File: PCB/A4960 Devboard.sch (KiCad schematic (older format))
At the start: 56 parts, among them IC1 ATMEGA8-AI, P1 CONN_02X03, P2 CONN_01X02, P3 CONN_01X03, P4 CONN_01X03, Q1 Q_NMOS_GDS_old, Q2 Q_NMOS_GDS_old, Q3 Q_NMOS_GDS_old, Q4 Q_NMOS_GDS_old, Q5 Q_NMOS_GDS_old, Q6 Q_NMOS_GDS_old, U1 LM2931AZ-5.0, U2 A4960, Y1 16MHz

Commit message: PCB weiter gemcht & neuer Spannungswandler auf 5V
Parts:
- removed U1: LM2931AZ-5.0, toni:SOT223_GND_VO_VI, symbol LM2931AZ-5.0
- added U1: LD1117S50TR, TO_SOT_Packages_SMD:SOT-223, symbol LD1117S50TR
- R13: footprint Resistors_SMD:R_0603 -> Resistors_SMD:R_2512
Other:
- moved on the sheet: R20
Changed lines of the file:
@@
 F 0 "R13" V 7380 4600 50  0000 C CNN
 F 1 "R" V 7300 4600 50  0000 C CNN
-F 2 "Resistors_SMD:R_0603" V 7230 4600 30  0001 C CNN
+F 2 "Resistors_SMD:R_2512" V 7230 4600 30  0001 C CNN
 F 3 "" H 7300 4600 30  0000 C CNN
 	1    7300 4600
@@
 $EndComp
 $Comp
-L LM2931AZ-5.0 U1
-U 1 1 5653AFAA
-P 2400 6725
-F 0 "U1" H 2400 6975 40  0000 C CNN
-F 1 "LM2931AZ-5.0" H 2400 6925 40  0000 C CNN
-F 2 "toni:SOT223_GND_VO_VI" H 2400 6825 35  0001 C CIN
-F 3 "" H 2400 6725 60  0000 C CNN
-	1    2400 6725
-	1    0    0    -1
-$EndComp
-$Comp
 L +3.3V #PWR050
 U 1 1 5653B466
-P 2800 6675
-F 0 "#PWR050" H 2800 6525 50  0001 C CNN
-F 1 "+3.3V" H 2800 6815 50  0000 C CNN
-F 2 "" H 2800 6675 60  0000 C CNN
-F 3 "" H 2800 6675 60  0000 C CNN
-	1    2800 6675
+P 2675 6125
+F 0 "#PWR050" H 2675 5975 50  0001 C CNN
+F 1 "+3.3V" H 2675 6265 50  0000 C CNN
+F 2 "" H 2675 6125 60  0000 C CNN
+F 3 "" H 2675 6125 60  0000 C CNN
+	1    2675 6125
 	1    0    0    -1
 $EndComp
@@
 L GND #PWR051
 U 1 1 5653BE8A
-P 2400 6975
-F 0 "#PWR051" H 2400 6725 50  0001 C CNN
-F 1 "GND" H 2400 6825 50  0000 C CNN
-F 2 "" H 2400 6975 60  0000 C CNN
-F 3 "" H 2400 6975 60  0000 C CNN
-	1    2400 6975
+P 2275 6425
+F 0 "#PWR051" H 2275 6175 50  0001 C CNN
+F 1 "GND" H 2275 6275 50  0000 C CNN
+F 2 "" H 2275 6425 60  0000 C CNN
+F 3 "" H 2275 6425 60  0000 C CNN
+	1    2275 6425
 	1    0    0    -1
 $EndComp
@@
 L VPP #PWR052
 U 1 1 5653BF3A
-P 1700 6675
-F 0 "#PWR052" H 1700 6525 50  0001 C CNN
-F 1 "VPP" H 1700 6825 50  0000 C CNN
-F 2 "" H 1700 6675 60  0000 C CNN
-F 3 "" H 1700 6675 60  0000 C CNN
-	1    1700 6675
+P 1575 6125
+F 0 "#PWR052" H 1575 5975 50  0001 C CNN
+F 1 "VPP" H 1575 6275 50  0000 C CNN
+F 2 "" H 1575 6125 60  0000 C CNN
+F 3 "" H 1575 6125 60  0000 C CNN
+	1    1575 6125
 	0    -1   -1   0
 $EndComp
@@
 L R R20
 U 1 1 5653BFEC
-P 1850 6675
-F 0 "R20" V 1930 6675 50  0000 C CNN
-F 1 "1" V 1850 6675 50  0000 C CNN
-F 2 "Resistors_SMD:R_0805" V 1780 6675 30  0001 C CNN
-F 3 "" H 1850 6675 30  0000 C CNN
-	1    1850 6675
+P 1725 6125
+F 0 "R20" V 1805 6125 50  0000 C CNN
+F 1 "1" V 1725 6125 50  0000 C CNN
+F 2 "Resistors_SMD:R_0805" V 1655 6125 30  0001 C CNN
+F 3 "" H 1725 6125 30  0000 C CNN
+	1    1725 6125
 	0    1    1    0
 $EndComp
@@
 $EndComp
 $Comp
-L +3.3V #PWR?
+L +3.3V #PWR054
 U 1 1 56577063
 P 4550 2950
-F 0 "#PWR?" H 4550 2800 50  0001 C CNN
+F 0 "#PWR054" H 4550 2800 50  0001 C CNN
 F 1 "+3.3V" H 4550 3090 50  0000 C CNN
 F 2 "" H 4550 2950 60  0000 C CNN
@@
 $EndComp
 Connection ~ 4600 2950
+$Comp
+L LD1117S50TR U1
+U 1 1 565871BF
+P 2275 6175
+F 0 "U1" H 2275 6425 40  0000 C CNN
+F 1 "LD1117S50TR" H 2275 6375 40  0000 C CNN
+F 2 "TO_SOT_Packages_SMD:SOT-223" H 2275 6275 40  0000 C CNN
+F 3 "" H 2275 6175 60  0000 C CNN
+	1    2275 6175
+	1    0    0    -1
+$EndComp
 $EndSCHEMATC

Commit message: PCB fertig!
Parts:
- Q1, Q2, Q3, Q4, Q5, Q6: footprint sven:SO8_WITH_Heatpipes -> Sven:SO8_WITH_Heatpipes_New
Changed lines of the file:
@@
 F 0 "Q1" H 9350 2750 50  0000 R CNN
 F 1 "Q_NMOS_GDS_old" H 9700 2650 50  0000 R CNN
-F 2 "sven:SO8_WITH_Heatpipes" H 9250 2800 29  0001 C CNN
+F 2 "Sven:SO8_WITH_Heatpipes_New" H 9250 2800 29  0001 C CNN
 F 3 "" H 9050 2700 60  0000 C CNN
 	1    9050 2700
@@
 F 0 "Q2" H 9350 3150 50  0000 R CNN
 F 1 "Q_NMOS_GDS_old" H 9700 3050 50  0000 R CNN
-F 2 "sven:SO8_WITH_Heatpipes" H 9250 3200 29  0001 C CNN
+F 2 "Sven:SO8_WITH_Heatpipes_New" H 9250 3200 29  0001 C CNN
 F 3 "" H 9050 3100 60  0000 C CNN
 	1    9050 3100
@@
 F 0 "Q3" H 9350 3850 50  0000 R CNN
 F 1 "Q_NMOS_GDS_old" H 9700 3750 50  0000 R CNN
-F 2 "sven:SO8_WITH_Heatpipes" H 9250 3900 29  0001 C CNN
+F 2 "Sven:SO8_WITH_Heatpipes_New" H 9250 3900 29  0001 C CNN
 F 3 "" H 9050 3800 60  0000 C CNN
 	1    9050 3800
@@
 F 0 "Q4" H 9350 4250 50  0000 R CNN
 F 1 "Q_NMOS_GDS_old" H 9700 4150 50  0000 R CNN
-F 2 "sven:SO8_WITH_Heatpipes" H 9250 4300 29  0001 C CNN
+F 2 "Sven:SO8_WITH_Heatpipes_New" H 9250 4300 29  0001 C CNN
 F 3 "" H 9050 4200 60  0000 C CNN
 	1    9050 4200
@@
 F 0 "Q5" H 9350 4950 50  0000 R CNN
 F 1 "Q_NMOS_GDS_old" H 9700 4850 50  0000 R CNN
-F 2 "sven:SO8_WITH_Heatpipes" H 9250 5000 29  0001 C CNN
+F 2 "Sven:SO8_WITH_Heatpipes_New" H 9250 5000 29  0001 C CNN
 F 3 "" H 9050 4900 60  0000 C CNN
 	1    9050 4900
@@
 F 0 "Q6" H 9350 5350 50  0000 R CNN
 F 1 "Q_NMOS_GDS_old" H 9700 5250 50  0000 R CNN
-F 2 "sven:SO8_WITH_Heatpipes" H 9250 5400 29  0001 C CNN
+F 2 "Sven:SO8_WITH_Heatpipes_New" H 9250 5400 29  0001 C CNN
 F 3 "" H 9050 5300 60  0000 C CNN
 	1    9050 5300

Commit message: Leiterplatte so gefertigt
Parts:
- R10: value R -> 5,6k
- R3: value R -> 22k
- R4: value R -> 2,2k
- R5, R8: value 100 -> 330
- R9: value R -> 10k
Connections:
- net MISO: now also P1.1 (P1); no longer P1.4 (P4)
- net MOSI: now also P1.4 (P4); no longer P1.1 (P1)
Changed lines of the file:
@@
 Text Label 4150 2500 0    60   ~ 0
 CS
-Text Label 1850 950  0    60   ~ 0
+Text Label 2950 1050 2    60   ~ 0
 MOSI
 Text Label 1850 1050 0    60   ~ 0
 SCK
-Text Label 2950 1050 2    60   ~ 0
+Text Label 1850 950  0    60   ~ 0
 MISO
 Text Label 1250 2400 0    60   ~ 0
@@
 P 3650 1000
 F 0 "R3" V 3730 1000 50  0000 C CNN
-F 1 "R" V 3650 1000 50  0000 C CNN
+F 1 "22k" V 3650 1000 50  0000 C CNN
 F 2 "Resistors_SMD:R_0603" V 3580 1000 30  0001 C CNN
 F 3 "" H 3650 1000 30  0000 C CNN
@@
 P 3650 1300
 F 0 "R4" V 3730 1300 50  0000 C CNN
-F 1 "R" V 3650 1300 50  0000 C CNN
+F 1 "2,2k" V 3650 1300 50  0000 C CNN
 F 2 "Resistors_SMD:R_0603" V 3580 1300 30  0001 C CNN
 F 3 "" H 3650 1300 30  0000 C CNN
@@
 P 4300 1000
 F 0 "R9" V 4380 1000 50  0000 C CNN
-F 1 "R" V 4300 1000 50  0000 C CNN
+F 1 "10k" V 4300 1000 50  0000 C CNN
 F 2 "Resistors_SMD:R_0603" V 4230 1000 30  0001 C CNN
 F 3 "" H 4300 1000 30  0000 C CNN
@@
 P 4300 1300
 F 0 "R10" V 4380 1300 50  0000 C CNN
-F 1 "R" V 4300 1300 50  0000 C CNN
+F 1 "5,6k" V 4300 1300 50  0000 C CNN
 F 2 "Resistors_SMD:R_0603" V 4230 1300 30  0001 C CNN
 F 3 "" H 4300 1300 30  0000 C CNN
@@
 P 3650 5350
 F 0 "R5" V 3730 5350 50  0000 C CNN
-F 1 "100" V 3650 5350 50  0000 C CNN
+F 1 "330" V 3650 5350 50  0000 C CNN
 F 2 "Resistors_SMD:R_0603" V 3580 5350 30  0001 C CNN
 F 3 "" H 3650 5350 30  0000 C CNN
@@
 P 3950 5350
 F 0 "R8" V 4030 5350 50  0000 C CNN
-F 1 "100" V 3950 5350 50  0000 C CNN
+F 1 "330" V 3950 5350 50  0000 C CNN
 F 2 "Resistors_SMD:R_0603" V 3880 5350 30  0001 C CNN
 F 3 "" H 3950 5350 30  0000 C CNN

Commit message: Pr0gramm angefangen, Umrichter versucht anzulaufen. aufspaltung in umrichter.h und umrichter.c, damit Ordnung herrscht.
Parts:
- D3: value LED -> grün
- D4: value LED -> rot
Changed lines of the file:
@@
 P 3650 5000
 F 0 "D3" H 3650 5100 50  0000 C CNN
-F 1 "LED" H 3650 4900 50  0000 C CNN
+F 1 "grün" H 3650 4900 50  0000 C CNN
 F 2 "LEDs:LED-0603" H 3650 5000 60  0001 C CNN
 F 3 "" H 3650 5000 60  0000 C CNN
@@
 P 3950 5000
 F 0 "D4" H 3950 5100 50  0000 C CNN
-F 1 "LED" H 3950 4900 50  0000 C CNN
+F 1 "rot" H 3950 4900 50  0000 C CNN
 F 2 "LEDs:LED-0603" H 3950 5000 60  0001 C CNN
 F 3 "" H 3950 5000 60  0000 C CNN

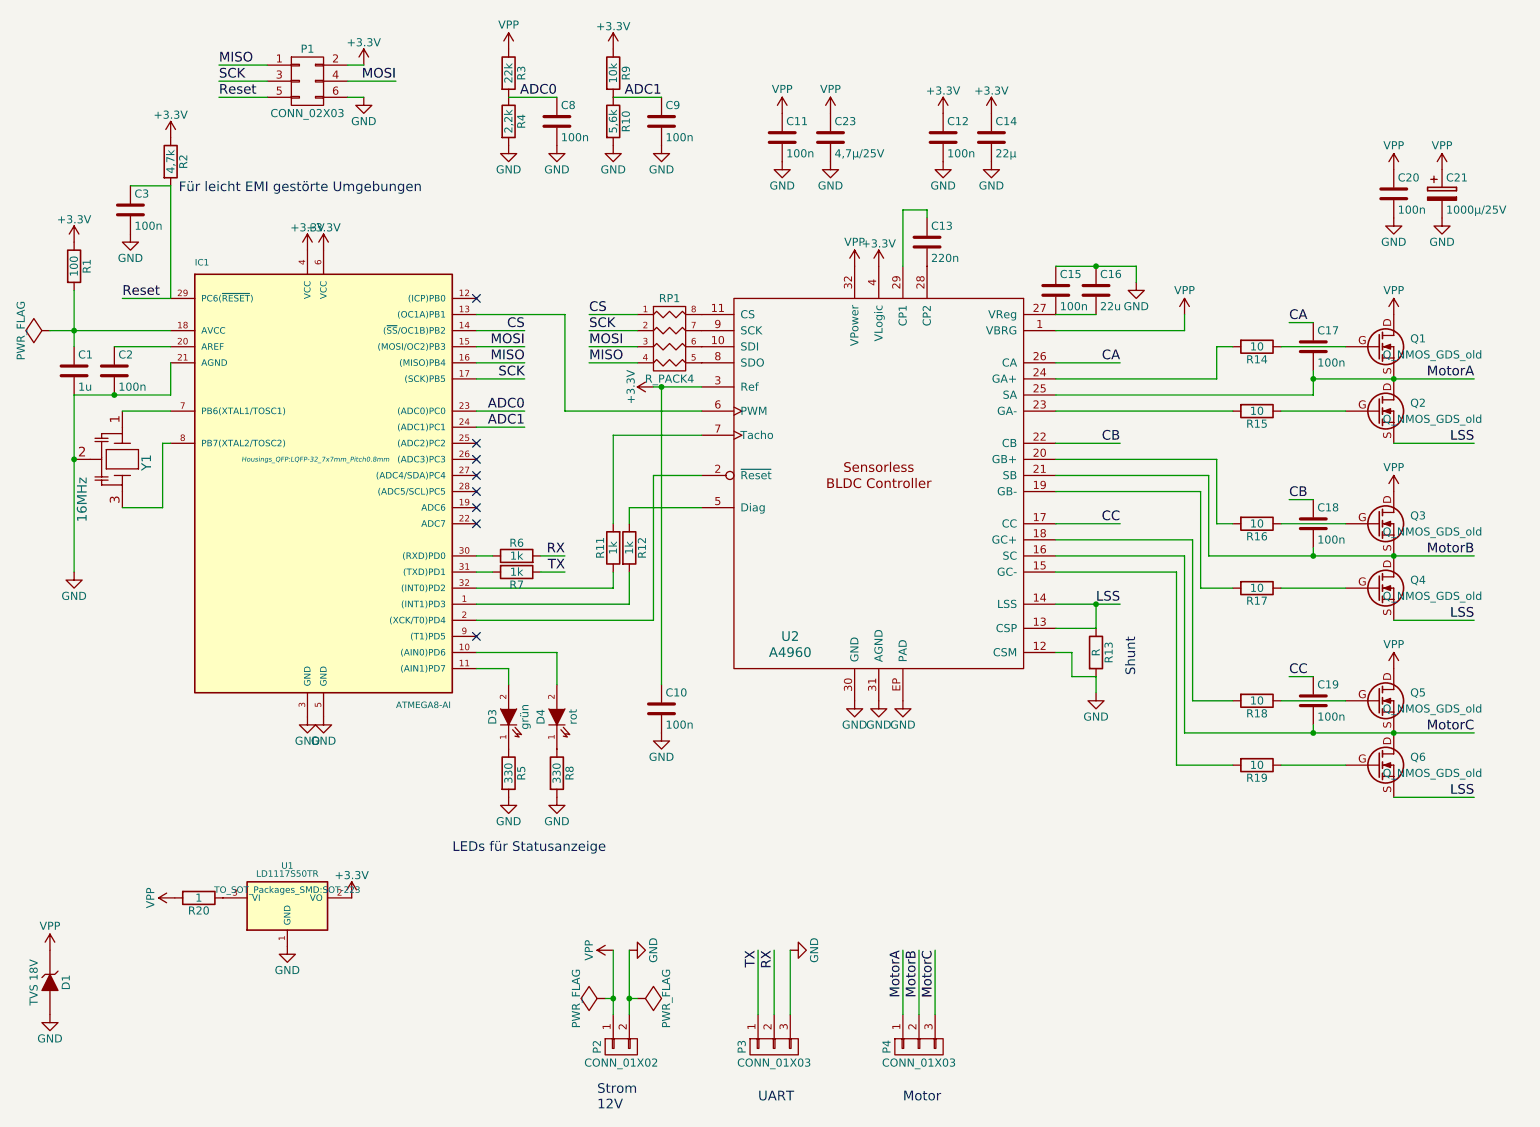
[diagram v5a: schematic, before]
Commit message: Schaltplan: fehlende Bauteilwerte eingetragen Programm: Motor läuft an. jetzt fehlen noch Regelung und diverse ADC/Timer-Auswertungen
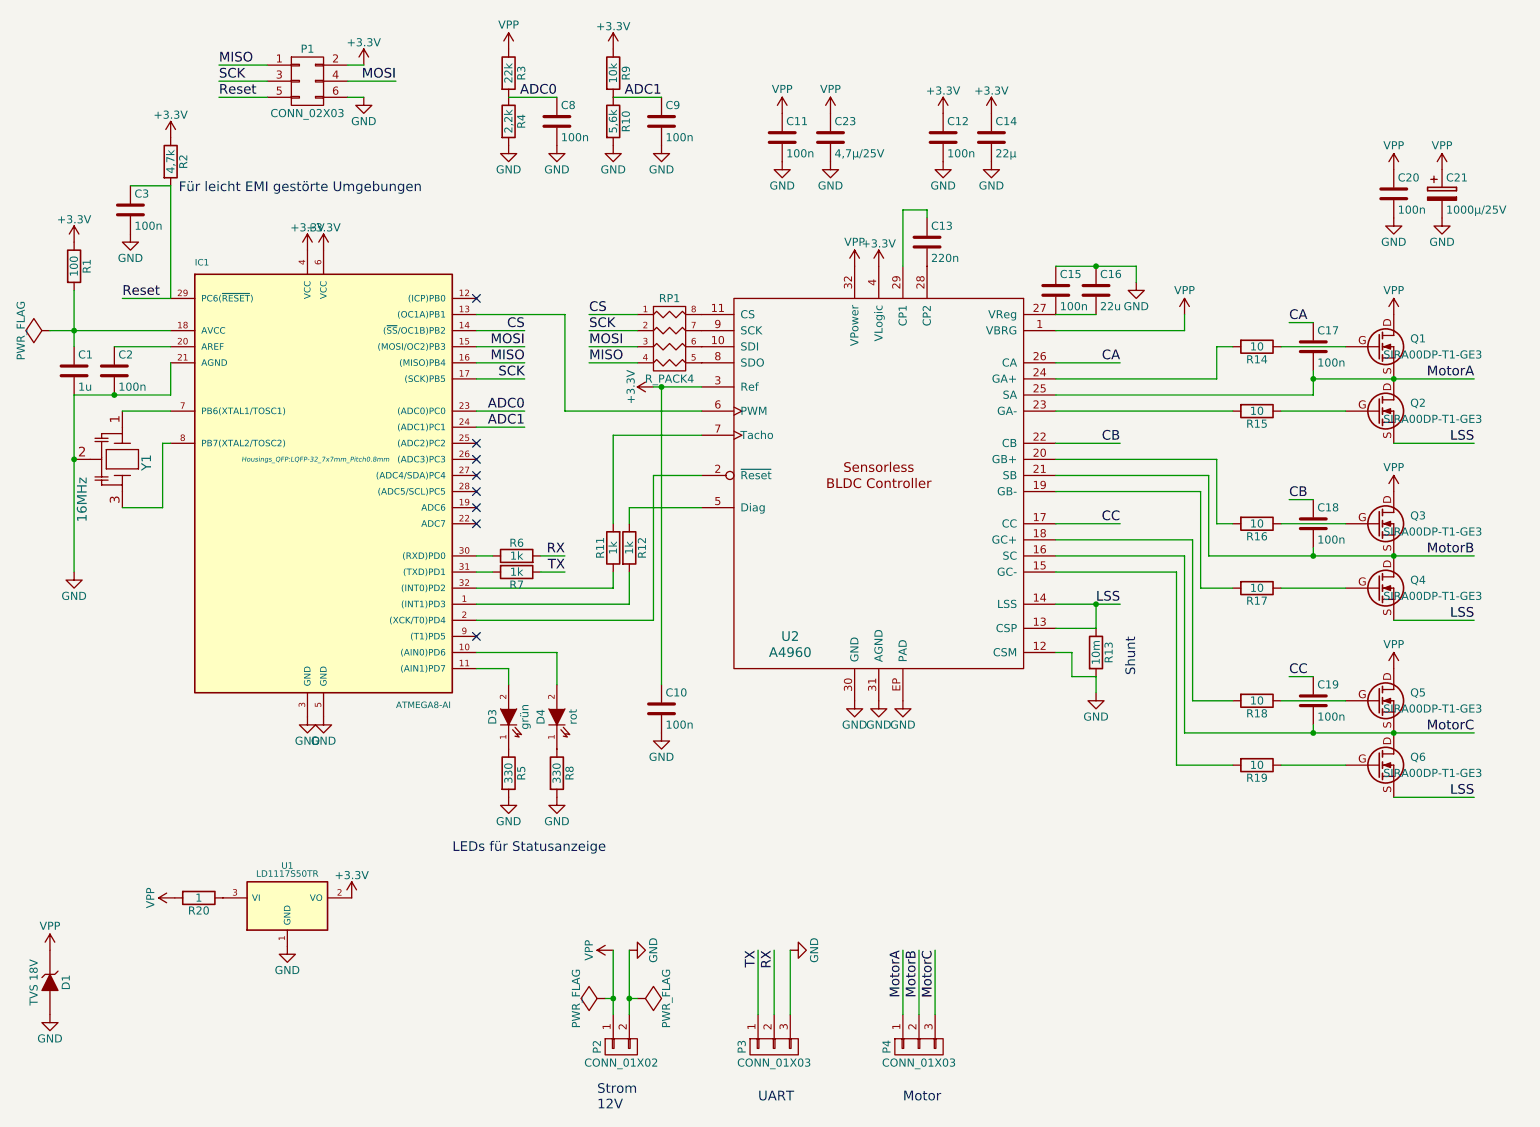
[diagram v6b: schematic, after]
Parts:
- Q1, Q2, Q3, Q4, Q5, Q6: value Q_NMOS_GDS_old -> SIRA00DP-T1-GE3
- R13: value R -> 10m; Digikey-Nummer (none) -> RHM.010AUCT-ND
- U2: Digikey-Nummer (none) -> 620-1452-1-ND
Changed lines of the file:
@@
 F 2 "Housings_QFP:TQFP-32_7x7mm_Pitch0.8mm" H 5400 2500 60  0001 C CNN
 F 3 "" H 5400 2500 60  0000 C CNN
+F 4 "620-1452-1-ND" H 5950 3550 60  0001 C CNN "Digikey-Nummer"
 	1    5950 3550
 	1    0    0    -1
@@
 P 7300 4600
 F 0 "R13" V 7380 4600 50  0000 C CNN
-F 1 "R" V 7300 4600 50  0000 C CNN
+F 1 "10m" V 7300 4600 50  0000 C CNN
 F 2 "Resistors_SMD:R_2512" V 7230 4600 30  0001 C CNN
 F 3 "" H 7300 4600 30  0000 C CNN
+F 4 "RHM.010AUCT-ND" V 7300 4600 60  0001 C CNN "Digikey-Nummer"
 	1    7300 4600
 	1    0    0    -1
@@
 P 9050 2700
 F 0 "Q1" H 9350 2750 50  0000 R CNN
-F 1 "Q_NMOS_GDS_old" H 9700 2650 50  0000 R CNN
+F 1 "SIRA00DP-T1-GE3" H 9700 2650 50  0000 R CNN
 F 2 "Sven:SO8_WITH_Heatpipes_New" H 9250 2800 29  0001 C CNN
 F 3 "" H 9050 2700 60  0000 C CNN
@@
 P 9050 3100
 F 0 "Q2" H 9350 3150 50  0000 R CNN
-F 1 "Q_NMOS_GDS_old" H 9700 3050 50  0000 R CNN
+F 1 "SIRA00DP-T1-GE3" H 9700 3050 50  0000 R CNN
 F 2 "Sven:SO8_WITH_Heatpipes_New" H 9250 3200 29  0001 C CNN
 F 3 "" H 9050 3100 60  0000 C CNN
@@
 P 9050 3800
 F 0 "Q3" H 9350 3850 50  0000 R CNN
-F 1 "Q_NMOS_GDS_old" H 9700 3750 50  0000 R CNN
+F 1 "SIRA00DP-T1-GE3" H 9700 3750 50  0000 R CNN
 F 2 "Sven:SO8_WITH_Heatpipes_New" H 9250 3900 29  0001 C CNN
 F 3 "" H 9050 3800 60  0000 C CNN
@@
 P 9050 4200
 F 0 "Q4" H 9350 4250 50  0000 R CNN
-F 1 "Q_NMOS_GDS_old" H 9700 4150 50  0000 R CNN
+F 1 "SIRA00DP-T1-GE3" H 9700 4150 50  0000 R CNN
 F 2 "Sven:SO8_WITH_Heatpipes_New" H 9250 4300 29  0001 C CNN
 F 3 "" H 9050 4200 60  0000 C CNN
@@
 P 9050 4900
 F 0 "Q5" H 9350 4950 50  0000 R CNN
-F 1 "Q_NMOS_GDS_old" H 9700 4850 50  0000 R CNN
+F 1 "SIRA00DP-T1-GE3" H 9700 4850 50  0000 R CNN
 F 2 "Sven:SO8_WITH_Heatpipes_New" H 9250 5000 29  0001 C CNN
 F 3 "" H 9050 4900 60  0000 C CNN
@@
 P 9050 5300
 F 0 "Q6" H 9350 5350 50  0000 R CNN
-F 1 "Q_NMOS_GDS_old" H 9700 5250 50  0000 R CNN
+F 1 "SIRA00DP-T1-GE3" H 9700 5250 50  0000 R CNN
 F 2 "Sven:SO8_WITH_Heatpipes_New" H 9250 5400 29  0001 C CNN
 F 3 "" H 9050 5300 60  0000 C CNN
@@
 F 0 "U1" H 2275 6425 40  0000 C CNN
 F 1 "LD1117S50TR" H 2275 6375 40  0000 C CNN
-F 2 "TO_SOT_Packages_SMD:SOT-223" H 2275 6275 40  0000 C CNN
+F 2 "TO_SOT_Packages_SMD:SOT-223" H 2275 6275 40  0001 C CNN
 F 3 "" H 2275 6175 60  0000 C CNN
 	1    2275 6175

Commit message: fehlende zwei Anschlüsse hinzugefügt.
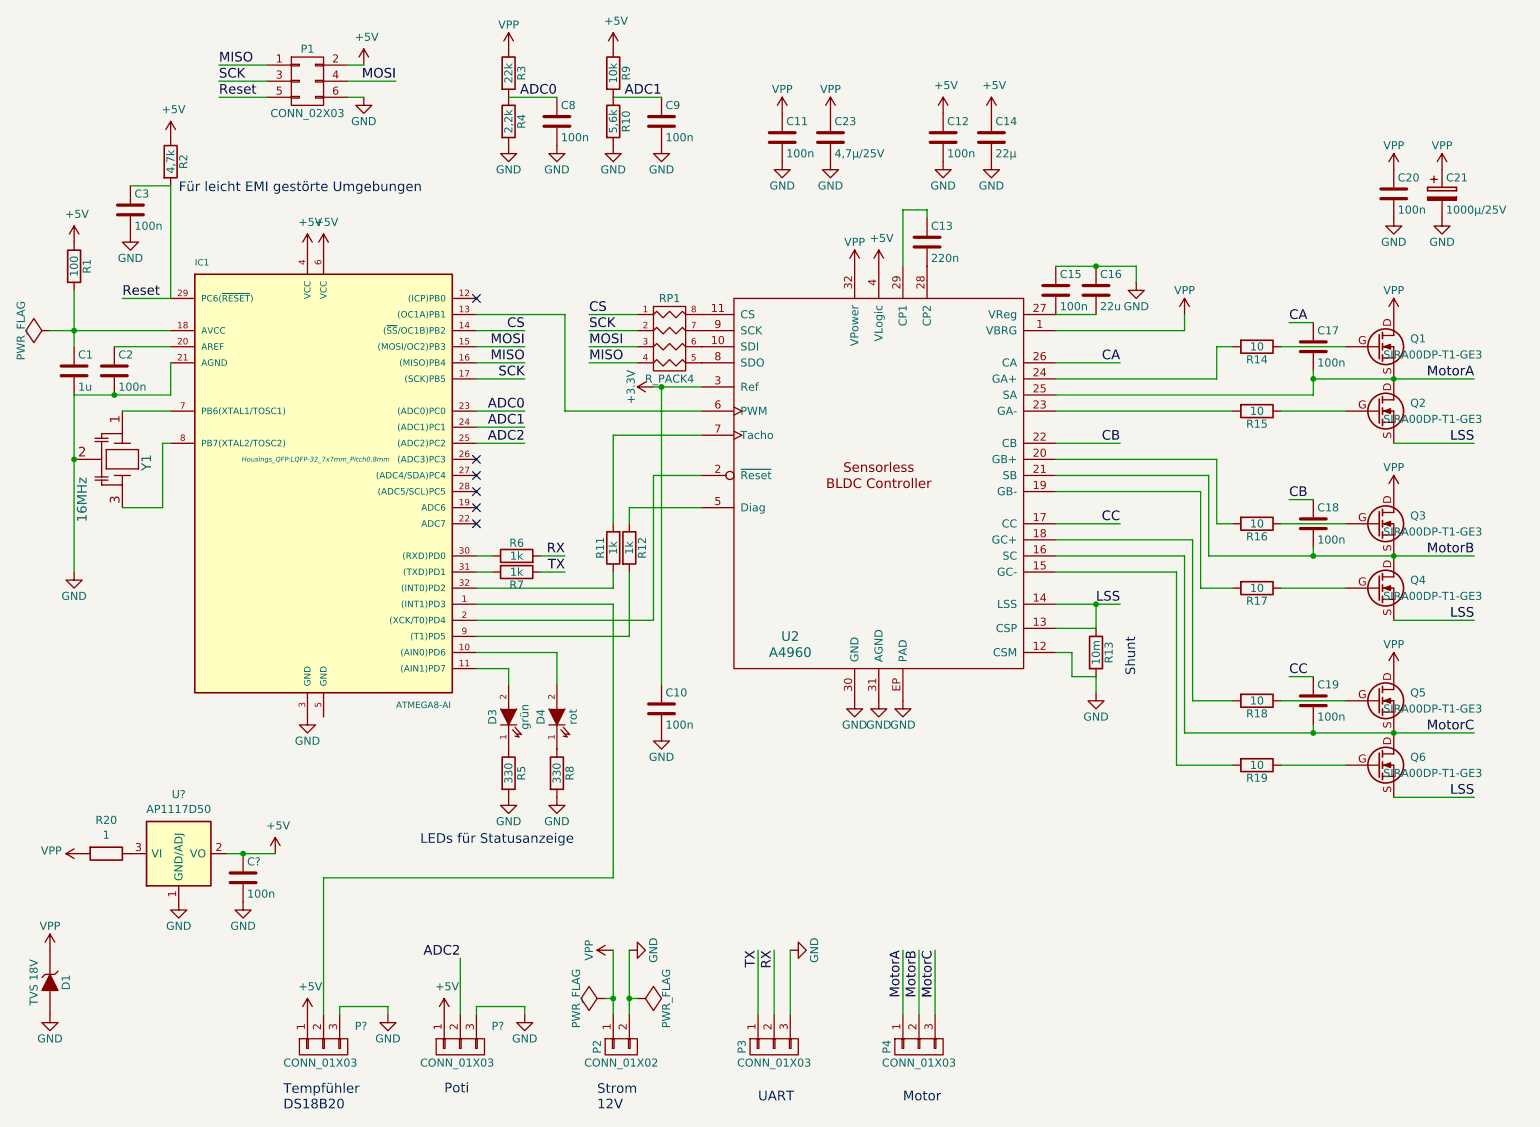
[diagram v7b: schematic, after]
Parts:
- removed U1: LD1117S50TR, TO_SOT_Packages_SMD:SOT-223, symbol LD1117S50TR
- added C?: 100n, Capacitors_SMD:C_0603, symbol C
- added P? (x2): CONN_01X03, symbol CONN_01X03
- added U?: AP1117D50, symbol AP1117D50
- R20: footprint Resistors_SMD:R_0805 -> (none)
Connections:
- net +3V3: no longer C12.1, C14.1, IC1.4 (VCC), IC1.6 (VCC), P1.2 (P2), R1.1, R2.1, R9.1, U2.4 (VLogic)
- net GND: now also C?.2, P?.3 (P3), P?.3 (P3), U?.1 (GND/ADJ); no longer IC1.5 (GND)
- net at IC1.1 ((INT1)PD3): now also P?.2 (P2); no longer R12.2
- net ADC2: now reaches IC1.25 ((ADC2)PC2)
- net ADC2: now also P?.2 (P2)
- net at IC1.9 ((T1)PD5): now also R12.2
- net at R20.1: now also U?.3 (VI)
- new net +5V: C12.1, C14.1, C?.1, IC1.4 (VCC), IC1.6 (VCC), P1.2 (P2), P?.1 (P1), P?.1 (P1), R1.1, R2.1, R9.1, U2.4 (VLogic), U?.2 (VO)
- no-connect marks 8 -> 6
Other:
- note added: "Poti"
- note added: "Tempfühler\nDS18B20"
